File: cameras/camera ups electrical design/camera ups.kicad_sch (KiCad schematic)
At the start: 20 parts, among them J1 COMPUTER_POWER_BUTTON, J2 VIDEO_SYSTEM_POWER_OUT, K1 RT42xAxx, Q1 Q_PMOS_DGS, Q2 NPN, U1 CD4541BE

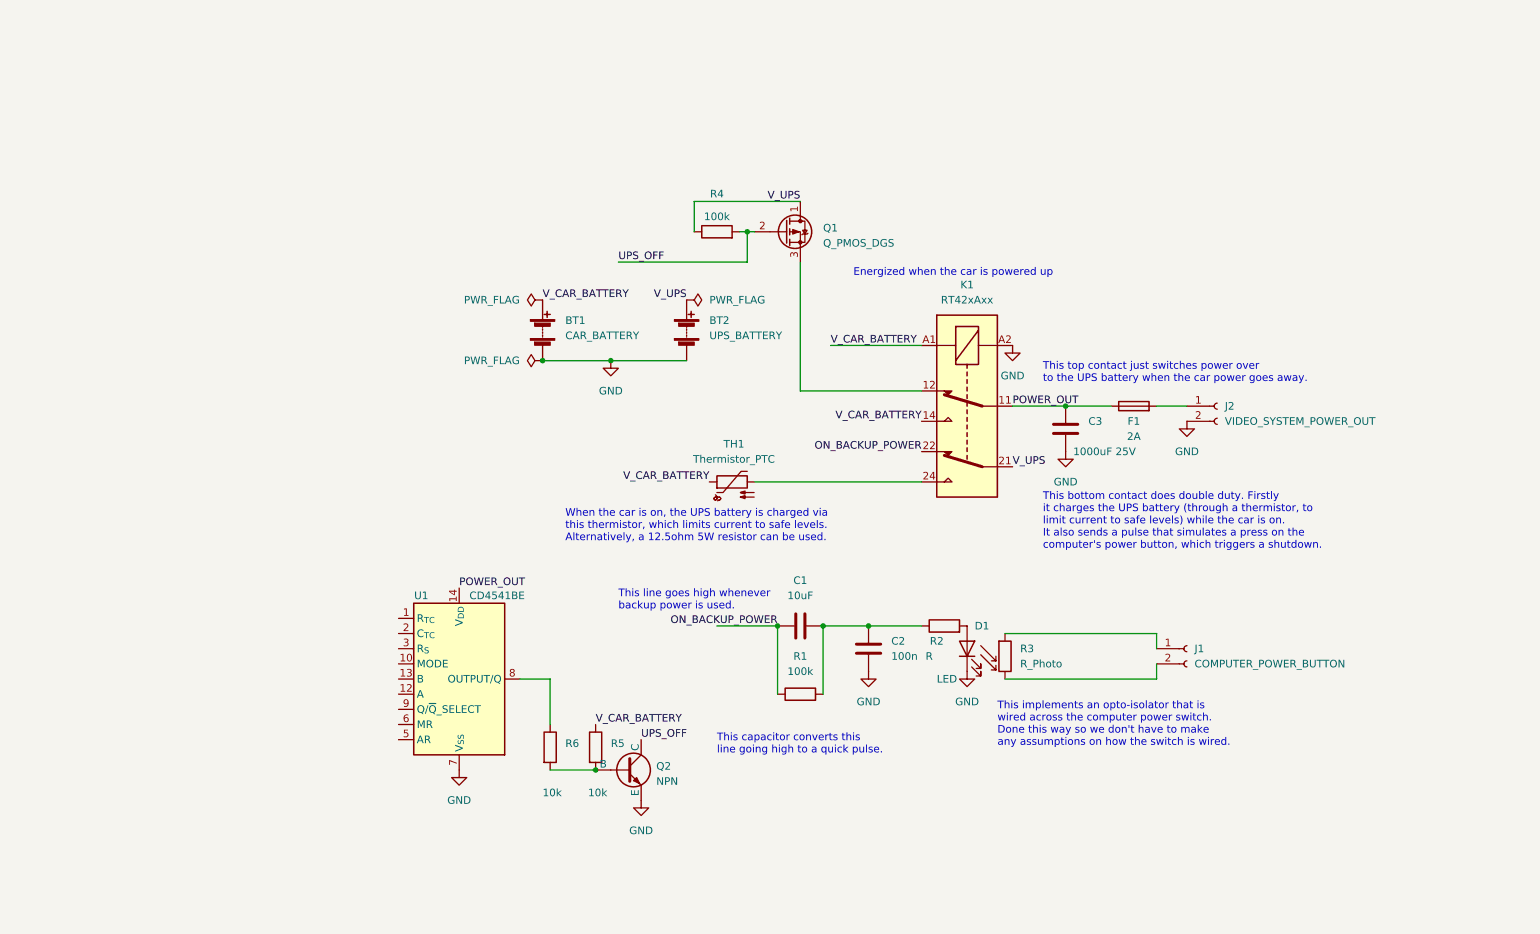
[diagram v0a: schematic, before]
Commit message: clean up ups circuit a bit
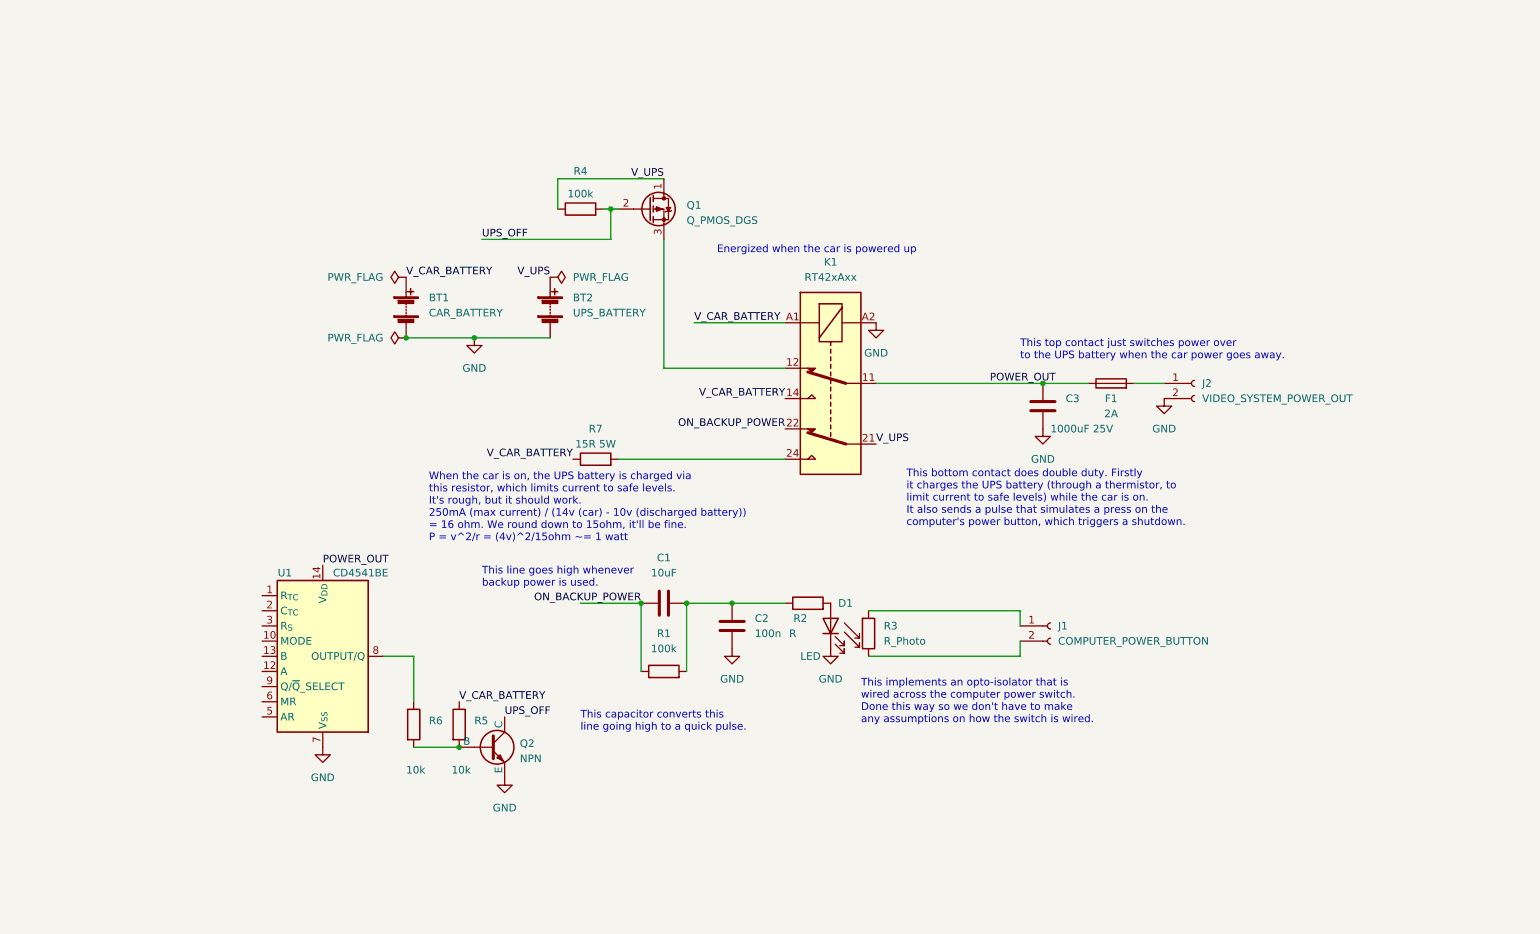
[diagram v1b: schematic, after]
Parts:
- removed TH1: Thermistor_PTC, symbol Device:Thermistor_PTC
- added R7: 15R 5W, symbol Device:R
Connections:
- net V_CAR_BATTERY: now also R7.1
- net at K1.24: now also R7.2
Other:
- note added: "When the car is on, the UPS battery is charged via this resistor, which limits current to safe levels. It's rough, but it should work. 250mA (max current) / (14v (car) - 10v (discharged battery)) = 16 ohm. We round down to 15ohm, it'll be fine. P = v^2/r = (4v)^2/15ohm ~= 1 watt"
- note removed: "When the car is on, the UPS battery is charged via this thermistor, which limits current to safe levels. Alternatively, a 12.5ohm 5W resistor can be used."
- moved on the sheet: BT1, BT2, C1, C2, C3, D1, F1, J1, J2, K1, Q1, Q2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

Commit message: vastly simplify ups circuit
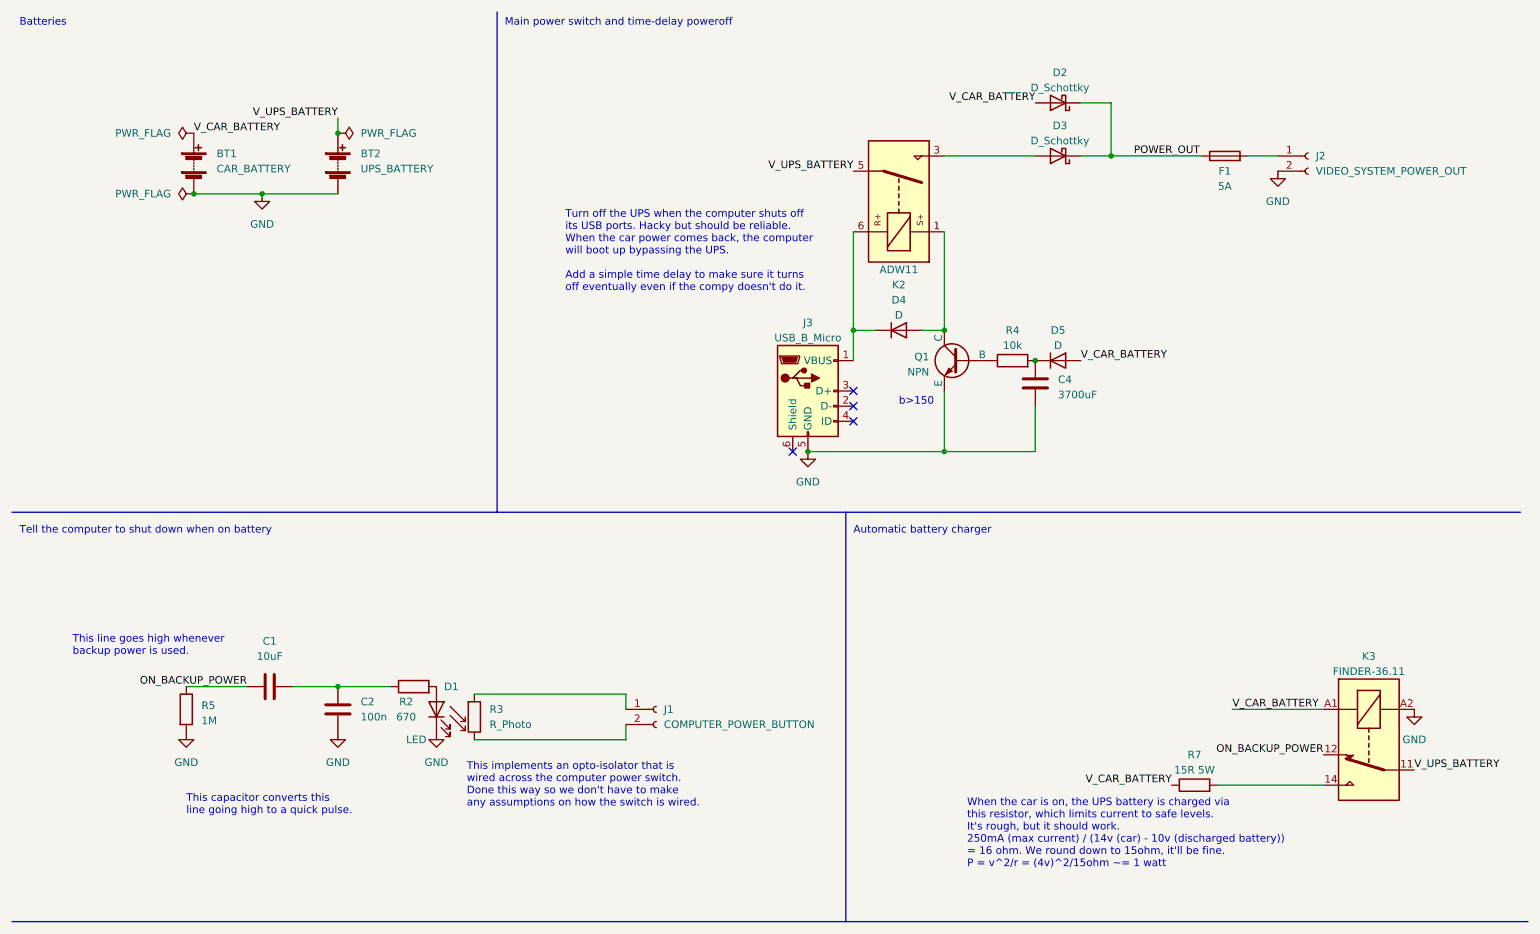
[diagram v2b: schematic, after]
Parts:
- removed C3: 1000uF 25V, symbol Device:C
- removed K1: RT42xAxx, Relay_THT:Relay_DPDT_Schrack-RT2-FormC_RM5mm, symbol Relay:RT42xAxx
- removed Q1: Q_PMOS_DGS, symbol Device:Q_PMOS_DGS
- removed Q2: NPN, symbol Simulation_SPICE:NPN
- removed R1: 100k, symbol Device:R
- removed R6: 10k, symbol Device:R
- removed U1: CD4541BE, Package_DIP:DIP-14_W7.62mm, symbol Timer:CD4541BE
- added C4: 3700uF, symbol Device:C
- added D2, D3: D_Schottky, symbol Device:D_Schottky
- added D4, D5: D, symbol Device:D
- added J3: USB_B_Micro, symbol Connector:USB_B_Micro
- added K2: ADW11, Relay_THT:Relay_1P1T_NO_10x24x18.8mm_Panasonic_ADW11xxxxW_THT, symbol Relay:ADW11
- added K3: FINDER-36.11, Relay_THT:Relay_SPDT_Finder_36.11, symbol Relay:FINDER-36.11
- added Q1: NPN, symbol Simulation_SPICE:NPN
- F1: value 2A -> 5A
- R2: value R -> 670
- R4: value 100k -> 10k
- R5: value 10k -> 1M
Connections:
- net GND: now also R5.2, C4.2, J3.5 (GND), K3.A2, Q1.3 (E)
- net ON_BACKUP_POWER: now also R5.1, K3.12
- net POWER_OUT: now also D2.1 (K), D3.1 (K)
- net V_CAR_BATTERY: now also D2.2 (A), D5.2 (A), K3.A1; no longer R5.1
- net at R7.2: now also K3.14
- net UPS_OFF: no longer names the net of R4.2
- net UPS_OFF: now also C4.1, D5.1 (K)
- net V_UPS: no longer names the net of R4.1
- net V_UPS: now also Q1.2 (B); no longer BT2.1 (+)
- new net: D4.1 (K), J3.1 (VBUS), K2.6
- new net: D4.2 (A), K2.1, Q1.1 (C)
- new net: D3.2 (A), K2.3
- new net V_UPS_BATTERY: BT2.1 (+), K2.5, K3.11
- no-connect marks 0 -> 4
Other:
- note added: "Automatic battery charger"
- note added: "Batteries"
- note added: "Main power switch and time-delay poweroff"
- note added: "Tell the computer to shut down when on battery"
- note added: "Turn off the UPS when the computer shuts off its USB ports. Hacky but should be reliable. When the car power comes back, the computer will boot up bypassing the UPS. Add a simple time delay to make sure it turns off eventually even if the compy doesn't do it."
- note added: "b>150"
- note removed: "Energized when the car is powered up"
- note removed: "This bottom contact does double duty. Firstly it charges the UPS battery (through a thermistor, to limit current to safe levels) while the car is on. It also sends a pulse that simulates a press on the computer's power button, which triggers a shutdown."
- note removed: "This top contact just switches power over to the UPS battery when the car power goes away."
- moved on the sheet: BT1, BT2, C1, C2, D1, F1, J1, J2, R2, R3, R7

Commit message: Use 12v relay for UPS switch.
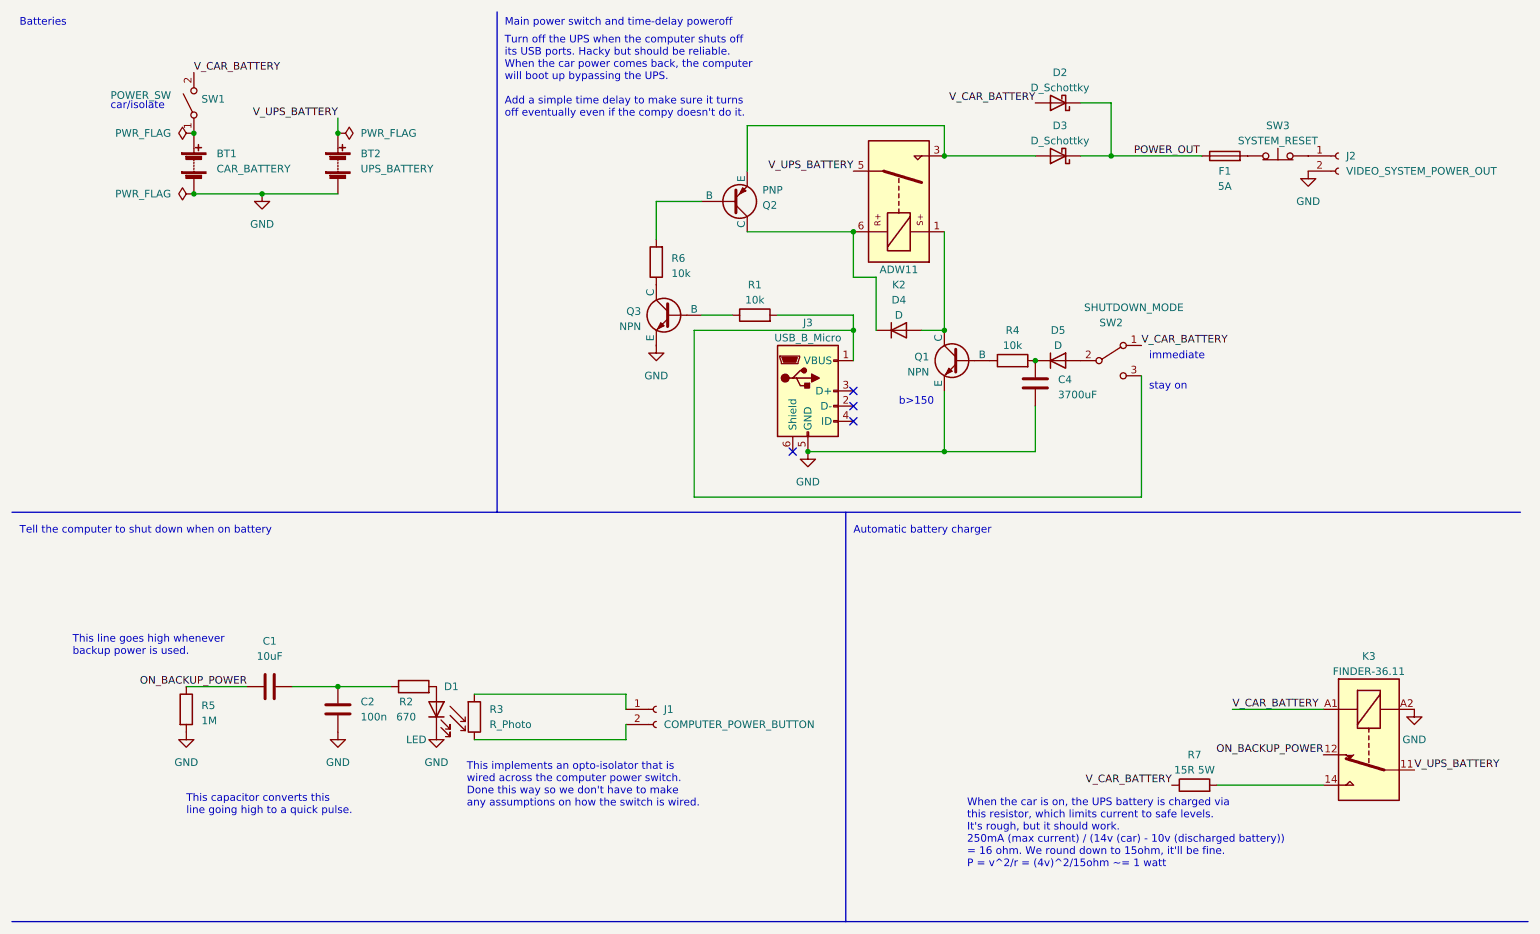
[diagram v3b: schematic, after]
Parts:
- added Q2: PNP, symbol Simulation_SPICE:PNP
- added Q3: NPN, symbol Simulation_SPICE:NPN
- added R1, R6: 10k, symbol Device:R
- added SW1: POWER_SW, symbol Switch:SW_SPST
- added SW2: SHUTDOWN_MODE, symbol Switch:SW_SPDT
- added SW3: SYSTEM_RESET, symbol Switch:SW_Push_Open
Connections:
- net GND: now also Q3.3 (E)
- net V_CAR_BATTERY: now also SW1.2 (B), SW2.1 (A); no longer BT1.1 (+), D5.2 (A)
- net at J2.1 (Pin_1): now also SW3.2 (B); no longer F1.2
- net at D4.1 (K), K2.6: now also Q2.1 (C); no longer J3.1 (VBUS)
- net at D3.2 (A), K2.3: now also Q2.3 (E)
- new net: BT1.1 (+), SW1.1 (A)
- new net: J3.1 (VBUS), R1.2, SW2.3 (C)
- new net: F1.2, SW3.1 (A)
- new net: D5.2 (A), SW2.2 (B)
- new net: Q2.2 (B), R6.2
- new net: Q3.2 (B), R1.1
- new net: Q3.1 (C), R6.1
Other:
- note added: "car/isolate"
- note added: "immediate"
- note added: "stay on"
- moved on the sheet: J2

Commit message: ups: simplify, correct computer poweroff circuit
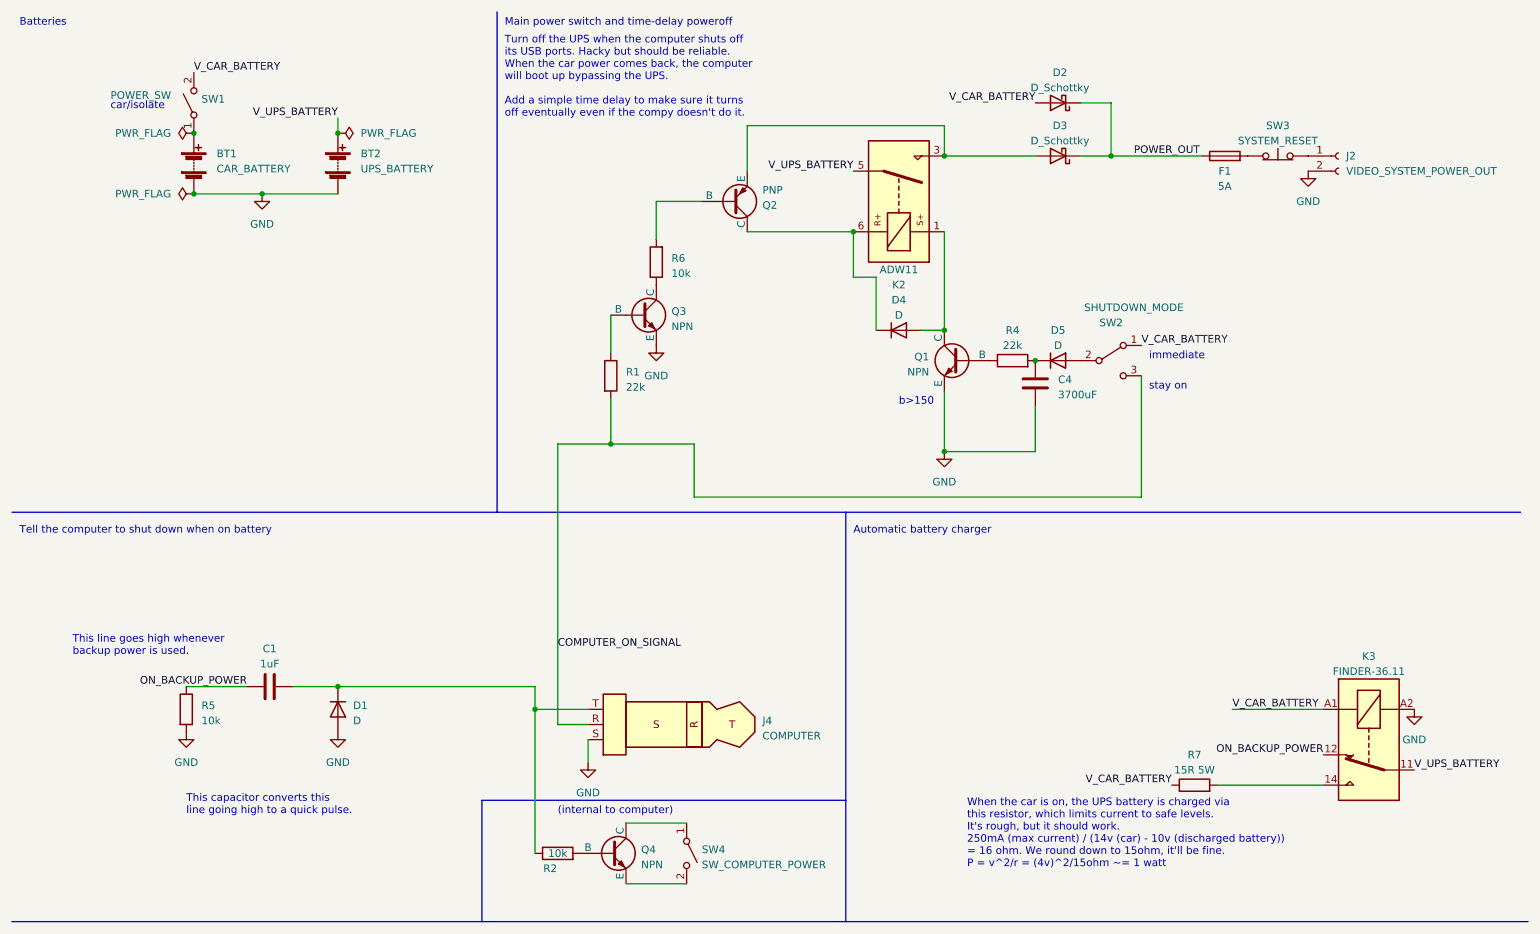
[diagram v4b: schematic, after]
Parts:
- removed C2: 100n, symbol Device:C
- removed D1: LED, symbol Device:LED
- removed J1: COMPUTER_POWER_BUTTON, symbol Connector:Conn_01x02_Female
- removed J3: USB_B_Micro, symbol Connector:USB_B_Micro
- removed R3: R_Photo, symbol Device:R_Photo
- added D1: D, symbol Device:D
- added J4: COMPUTER, symbol Connector_Audio:AudioPlug3
- added Q4: NPN, symbol Simulation_SPICE:NPN
- added SW4: SW_COMPUTER_POWER, symbol Switch:SW_SPST
- C1: value 10uF -> 1uF
- R1, R4: value 10k -> 22k
- R2: value 670 -> 10k
- R5: value 1M -> 10k
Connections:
- net GND: now also D1.2 (A), J4.S
- net at C1.2, R2.1: now also D1.1 (K), J4.T
- net COMPUTER_ON_SIGNAL: now reaches R1.2, SW2.3 (C)
- net COMPUTER_ON_SIGNAL: now also J4.R
- net at R2.2: now also Q4.2 (B)
- new net: Q4.1 (C), SW4.1 (A)
- new net: Q4.3 (E), SW4.2 (B)
- no-connect marks 4 -> 0
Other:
- note added: "(internal to computer)"
- note removed: "This implements an opto-isolator that is wired across the computer power switch. Done this way so we don't have to make any assumptions on how the switch is wired."
- moved on the sheet: Q3, R1, R2

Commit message: UPS: more fixes
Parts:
- removed SW2: SHUTDOWN_MODE, symbol Switch:SW_SPDT
- added D6: LED, symbol Device:LED
- added R3: 560, symbol Device:R
- added R8: 10, symbol Device:R
- added SW5: SW_DPDT, symbol Switch:SW_DPDT_x2
- R1: value 22k -> 27k
- R4: value 22k -> 10k
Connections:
- net COMPUTER_ON_SIGNAL: now also SW5.3 (C)
- net ON_BACKUP_POWER: now also SW5.4 (A); no longer C1.1, R5.1
- net V_CAR_BATTERY: now also SW5.1 (A)
- net at D5.2 (A): now also R8.1
- net at D4.1 (K), K2.6, Q2.1 (C): now also D6.2 (A)
- net at D4.2 (A), K2.1, Q1.1 (C): now also R3.2
- new net: D6.1 (K), R3.1
- new net: C1.1, R5.1, SW5.5 (B)
- new net: R8.2, SW5.2 (B)
- no-connect marks 0 -> 1
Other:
- note added: "Timeout Circuit"
- note added: "red"
- note added: "ylw"
